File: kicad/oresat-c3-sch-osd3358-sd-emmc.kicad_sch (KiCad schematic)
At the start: 41 parts, among them J5 DM3BT-DSF-PEJS, U1 OSD3358-512M-BSM, U8 TCAN330, U9 EMMC+RESET+5.1-COMPATIBLE-BA

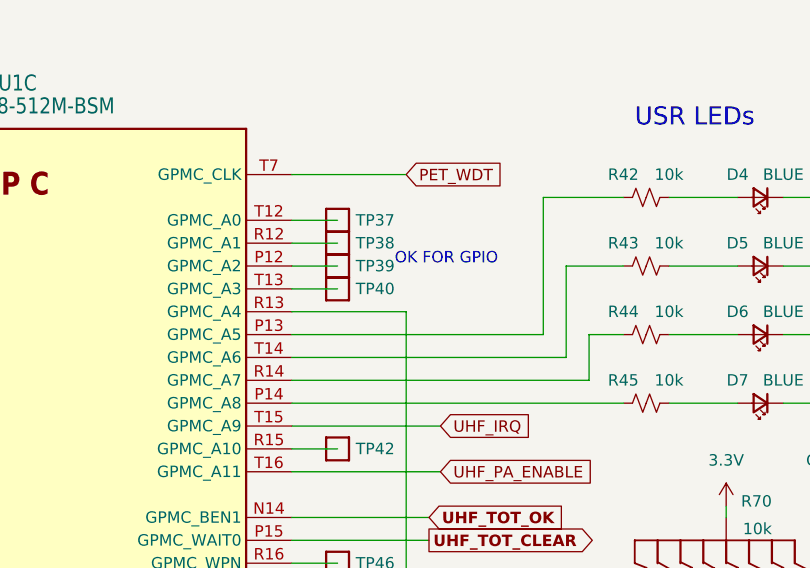
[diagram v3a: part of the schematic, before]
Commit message: routed everything but some minor lines and the radios. About to move the octavo and EVERYTHING else, wish me luck. Should give enough room for the radios!
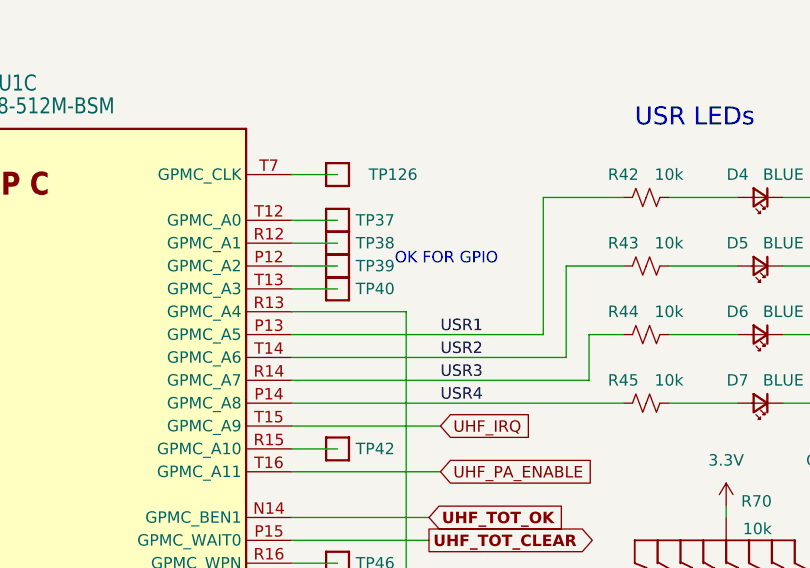
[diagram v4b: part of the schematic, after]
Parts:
- added TP126: Test-Point, oresat-misc:TestPoint_Pad_D1.0mm, symbol oresat-misc:Test-Point-1mm-round
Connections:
- net USR3: now reaches R44.1, U1.R14 (GPMC_A7)
- net USR1: now reaches R42.1, U1.P13 (GPMC_A5)
- net USR4: now reaches R45.1, U1.P14 (GPMC_A8)
- net USR2: now reaches R43.1, U1.T14 (GPMC_A6)
- net PET_WDT: no longer names the net of U1.T7 (GPMC_CLK)
- net PET_WDT: now also TP126.1
- new net: U9.A1 (NC), U9.A10 (NC), U9.A11 (NC), U9.A12 (NC), U9.A13 (NC), U9.A14 (NC), U9.A2 (NC), U9.A7 (NC), U9.A8 (NC), U9.A9 (NC)
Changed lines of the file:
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@@
+    (stroke (width 0) (type default))
+  )
+  (wire (pts (xy 223.52 101.6) (xy 228.6 101.6))
     (stroke (width 0) (type default))
   )
@@
   )
   (wire (pts (xy 101.6 129.54) (xy 83.82 129.54))
-    (stroke (width 0) (type default))
-  )
-  (wire (pts (xy 223.52 101.6) (xy 236.22 101.6))
     (stroke (width 0) (type default))
   )
@@
     (effects (font (size 1.27 1.27)) (justify left bottom))
   )
+  (label "USR3" (at 240.03 124.46 0) (fields_autoplaced)
+    (effects (font (size 1.27 1.27)) (justify left bottom))
+  )
+  (label "USR4" (at 240.03 127 0) (fields_autoplaced)
+    (effects (font (size 1.27 1.27)) (justify left bottom))
+  )
+  (label "USR2" (at 240.03 121.92 0) (fields_autoplaced)
+    (effects (font (size 1.27 1.27)) (justify left bottom))
+  )
+  (label "USR1" (at 240.03 119.38 0) (fields_autoplaced)
+    (effects (font (size 1.27 1.27)) (justify left bottom))
+  )
   (global_label "SPI1_CS" (shape input) (at 132.08 195.58 180) (fields_autoplaced)
     (effects (font (size 1.27 1.27)) (justify right))
@@
     (property "Intersheetrefs" "${INTERSHEET_REFS}" (at 138.3666 106.68 0)
       (effects (font (size 1.27 1.27)) (justify right))
-    )
-  )
-  (global_label "PET_WDT" (shape input) (at 236.22 101.6 0) (fields_autoplaced)
-    (effects (font (size 1.27 1.27)) (justify left))
-    (property "Intersheetrefs" "${INTERSHEET_REFS}" (at 247.169 101.6 0)
-      (effects (font (size 1.27 1.27)) (justify left))
     )
   )
@@
     )
   )
+  (symbol (lib_id "oresat-misc:Test-Point-1mm-round") (at 228.6 101.6 90) (unit 1)
+    (in_bom yes) (on_board yes) (dnp no)
+    (property "Reference" "TP126" (at 237.49 101.6 90)
+      (effects (font (size 1.27 1.27)) (justify left))
+    )
+    (property "Value" "Test-Point" (at 226.06 101.6 0)
+      (effects (font (size 1.27 1.27)) hide)
+    )
+    (property "Footprint" "oresat-misc:TestPoint_Pad_D1.0mm" (at 218.44 101.6 0)
+      (effects (font (size 1.27 1.27)) hide)
+    )
+    (property "Datasheet" "" (at 228.6 101.6 0)
+      (effects (font (size 1.27 1.27)) hide)
+    )
+    (pin "1")
+    (instances
+      (project "oresat-c3"
+        (path "/65d12cdd-c326-4033-9053-c59fa4e0b25e/0c732c1e-ab0d-41ac-9d77-9d7763333b6f"
+          (reference "TP126") (unit 1)
+        )
+        (path "/65d12cdd-c326-4033-9053-c59fa4e0b25e/f3d147ad-4cea-4d77-ae60-95882b03454e"
+          (reference "TP68") (unit 1)
+        )
+      )
+    )
+  )
   (symbol (lib_id "power:GND1") (at 55.88 153.67 0) (unit 1)
     (in_bom yes) (on_board yes) (dnp no)
@@
       (effects (font (size 1.27 1.27)) hide)
     )
+    (pin "A1")
+    (pin "A10")
+    (pin "A11")
+    (pin "A12")
+    (pin "A13")
+    (pin "A14")
+    (pin "A2")
     (pin "A3")
     (pin "A4")
     (pin "A5")
     (pin "A6")
+    (pin "A7")
+    (pin "A9")
     (pin "B2")
     (pin "B3")
@@
     (pin "P5")
     (pin "P6")
-    (instances
-      (project "oresat-c3"
+    (pin "A8")
+    (instances
+      (project "oresat-c3"

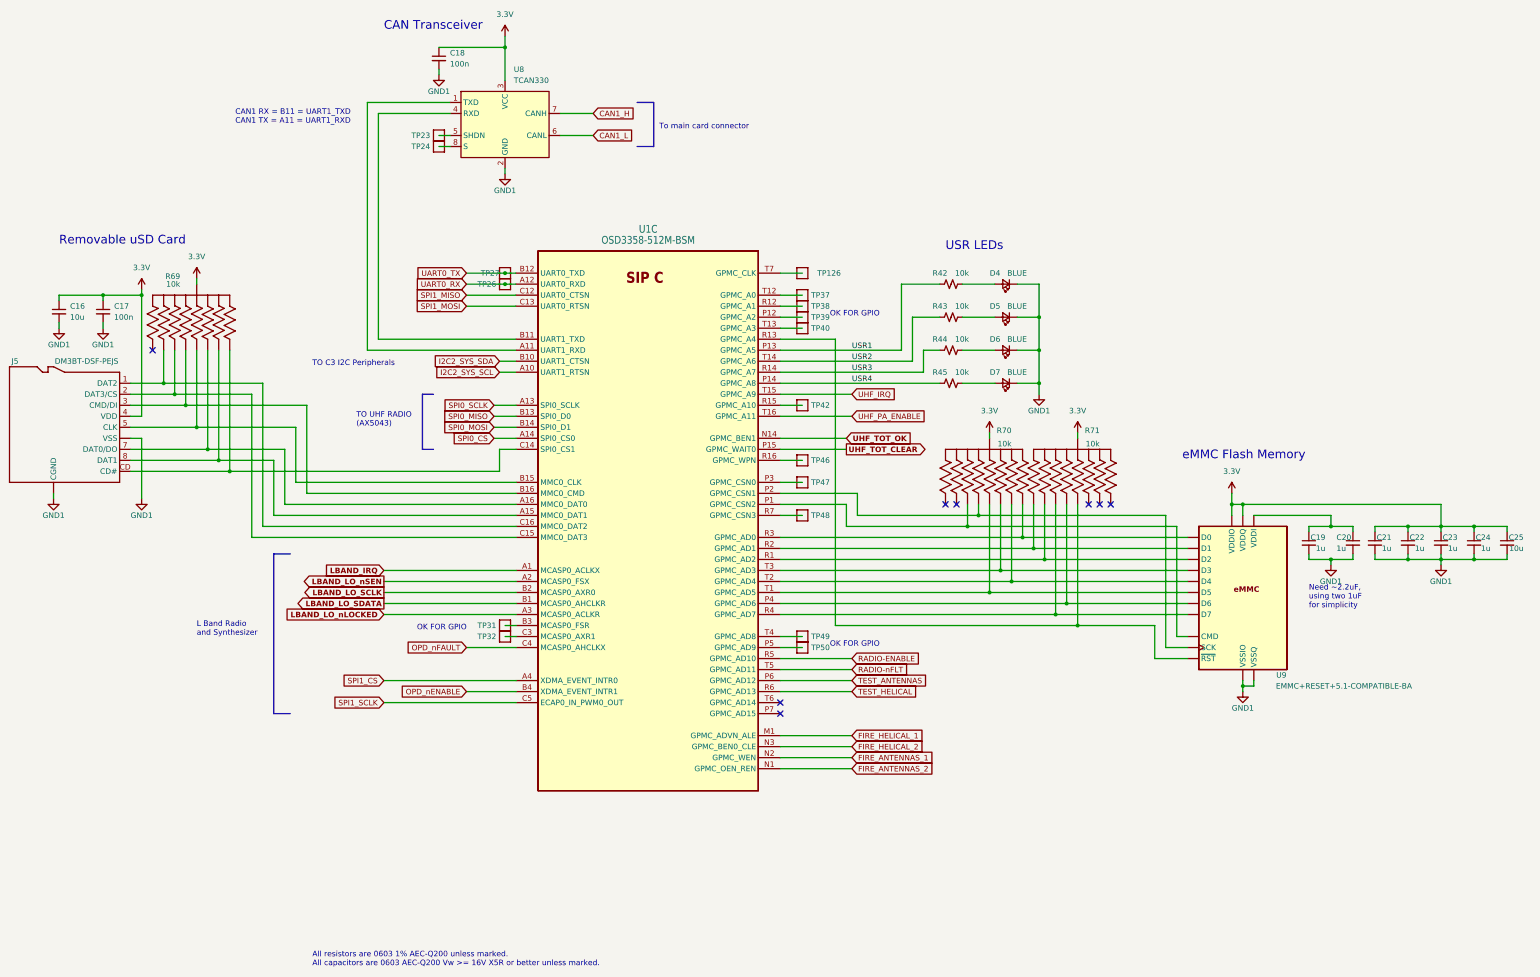
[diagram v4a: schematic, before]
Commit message: Switched all grounds to a single ground, because I can't find a way to overlap ground planes in KiCAD. That's actually not terrible, however, because KiCAD has an anti-plane feature which I used to cut the ground plane between UHF and L radios and L radio and Octavo. So actually I think it came out better than having separate ground planes. Only thing left now are the ~ 40 connections to the Octavo.
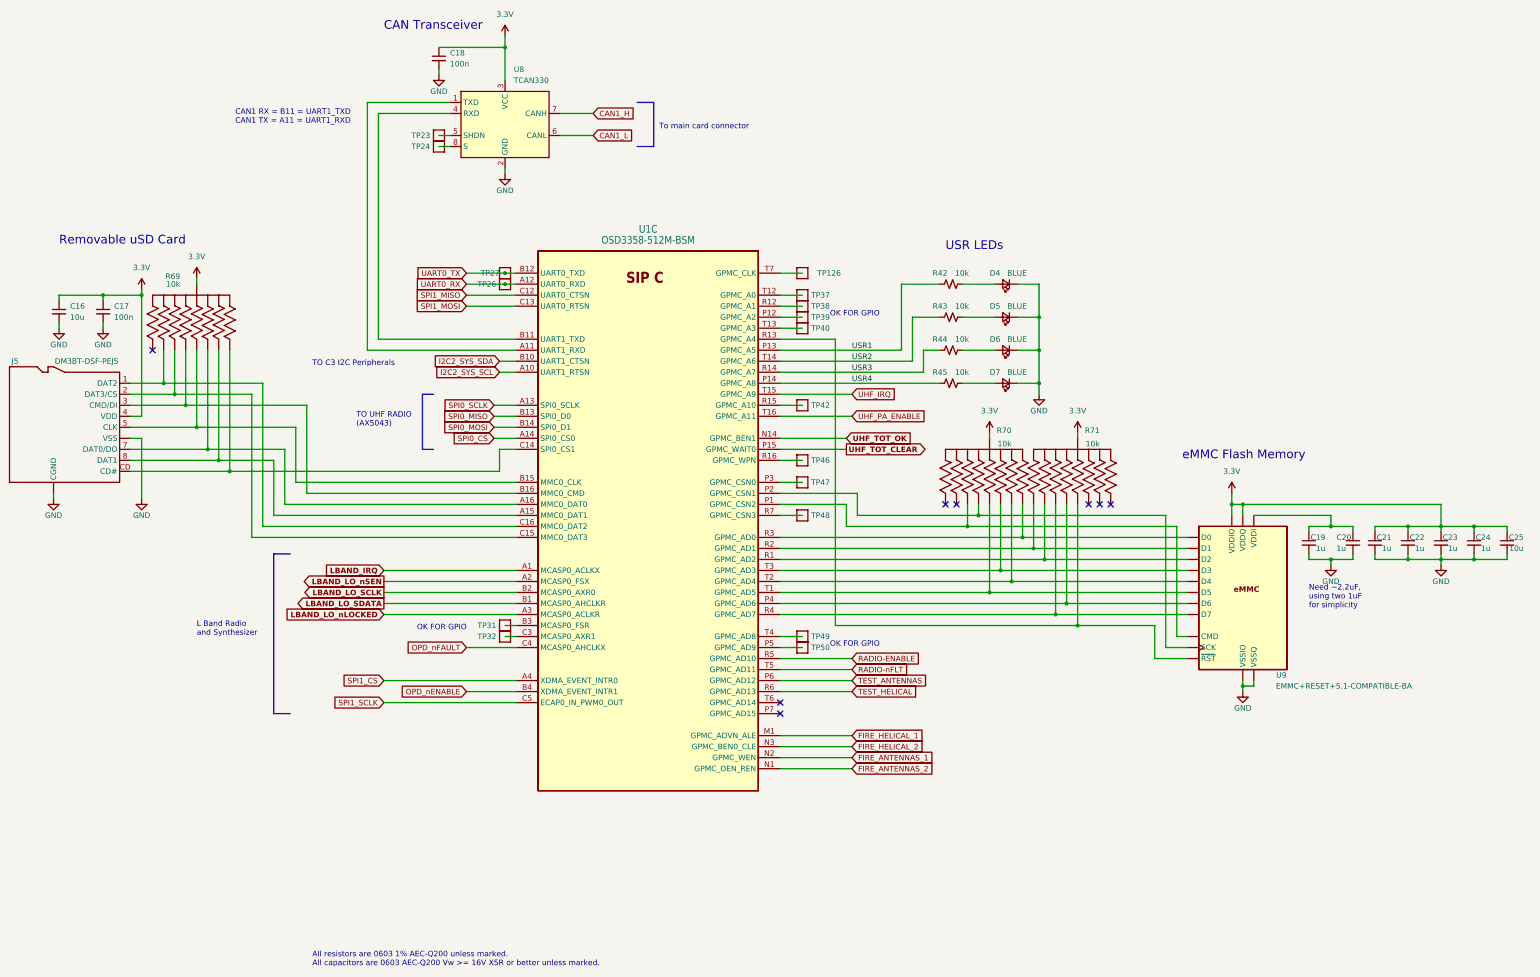
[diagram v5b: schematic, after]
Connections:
- net GND1 renamed GND
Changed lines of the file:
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@@
     )
   )
-  (symbol (lib_id "power:GND1") (at 375.92 168.91 0) (unit 1)
-    (in_bom yes) (on_board yes) (dnp no)
-    (property "Reference" "#PWR0149" (at 375.92 175.26 0)
-      (effects (font (size 1.27 1.27)) hide)
-    )
-    (property "Value" "GND1" (at 375.92 172.72 0)
+  (symbol (lib_id "power:GND") (at 375.92 168.91 0) (unit 1)
+    (in_bom yes) (on_board yes) (dnp no)
+    (property "Reference" "#PWR?" (at 375.92 175.26 0)
+      (effects (font (size 1.27 1.27)) hide)
+    )
+    (property "Value" "GND" (at 375.92 172.72 0)
       (effects (font (size 1.27 1.27)))
     )
@@
       (project "oresat-c3"
         (path "/65d12cdd-c326-4033-9053-c59fa4e0b25e/f3d147ad-4cea-4d77-ae60-95882b03454e"
-          (reference "#PWR0149") (unit 1)
+          (reference "#PWR?") (unit 1)
         )
       )
@@
     )
   )
-  (symbol (lib_id "power:GND1") (at 55.88 153.67 0) (unit 1)
-    (in_bom yes) (on_board yes) (dnp no)
-    (property "Reference" "#PWR0155" (at 55.88 160.02 0)
-      (effects (font (size 1.27 1.27)) hide)
-    )
-    (property "Value" "GND1" (at 55.88 157.48 0)
+  (symbol (lib_id "power:GND") (at 55.88 153.67 0) (unit 1)
+    (in_bom yes) (on_board yes) (dnp no)
+    (property "Reference" "#PWR?" (at 55.88 160.02 0)
+      (effects (font (size 1.27 1.27)) hide)
+    )
+    (property "Value" "GND" (at 55.88 157.48 0)
       (effects (font (size 1.27 1.27)))
     )
@@
       (project "oresat-c3"
         (path "/65d12cdd-c326-4033-9053-c59fa4e0b25e/f3d147ad-4cea-4d77-ae60-95882b03454e"
-          (reference "#PWR0155") (unit 1)
+          (reference "#PWR?") (unit 1)
         )
       )
@@
     )
   )
-  (symbol (lib_id "power:GND1") (at 283.21 129.54 0) (unit 1)
+  (symbol (lib_id "power:GND") (at 283.21 129.54 0) (unit 1)
     (in_bom yes) (on_board yes) (dnp no) (fields_autoplaced)
-    (property "Reference" "#PWR0148" (at 283.21 135.89 0)
-      (effects (font (size 1.27 1.27)) hide)
-    )
-    (property "Value" "GND1" (at 283.21 133.35 0)
+    (property "Reference" "#PWR?" (at 283.21 135.89 0)
+      (effects (font (size 1.27 1.27)) hide)
+    )
+    (property "Value" "GND" (at 283.21 133.35 0)
       (effects (font (size 1.27 1.27)))
     )
@@
       (project "oresat-c3"
         (path "/65d12cdd-c326-4033-9053-c59fa4e0b25e/f3d147ad-4cea-4d77-ae60-95882b03454e"
-          (reference "#PWR0148") (unit 1)
-        )
-      )
-    )
-  )
-  (symbol (lib_id "power:GND1") (at 76.2 153.67 0) (unit 1)
-    (in_bom yes) (on_board yes) (dnp no)
-    (property "Reference" "#PWR0156" (at 76.2 160.02 0)
-      (effects (font (size 1.27 1.27)) hide)
-    )
-    (property "Value" "GND1" (at 76.2 157.48 0)
+          (reference "#PWR?") (unit 1)
+        )
+      )
+    )
+  )
+  (symbol (lib_id "power:GND") (at 76.2 153.67 0) (unit 1)
+    (in_bom yes) (on_board yes) (dnp no)
+    (property "Reference" "#PWR?" (at 76.2 160.02 0)
+      (effects (font (size 1.27 1.27)) hide)
+    )
+    (property "Value" "GND" (at 76.2 157.48 0)
       (effects (font (size 1.27 1.27)))
     )
@@
       (project "oresat-c3"
         (path "/65d12cdd-c326-4033-9053-c59fa4e0b25e/f3d147ad-4cea-4d77-ae60-95882b03454e"
-          (reference "#PWR0156") (unit 1)
+          (reference "#PWR?") (unit 1)
         )
       )
@@
     )
   )
-  (symbol (lib_id "power:GND1") (at 350.52 168.91 0) (unit 1)
-    (in_bom yes) (on_board yes) (dnp no)
-    (property "Reference" "#PWR0151" (at 350.52 175.26 0)
-      (effects (font (size 1.27 1.27)) hide)
-    )
-    (property "Value" "GND1" (at 350.52 172.72 0)
+  (symbol (lib_id "power:GND") (at 350.52 168.91 0) (unit 1)
+    (in_bom yes) (on_board yes) (dnp no)
+    (property "Reference" "#PWR?" (at 350.52 175.26 0)
+      (effects (font (size 1.27 1.27)) hide)
+    )
+    (property "Value" "GND" (at 350.52 172.72 0)
       (effects (font (size 1.27 1.27)))
     )
@@
       (project "oresat-c3"
         (path "/65d12cdd-c326-4033-9053-c59fa4e0b25e/f3d147ad-4cea-4d77-ae60-95882b03454e"
-          (reference "#PWR0151") (unit 1)
-        )
-      )
-    )
-  )
-  (symbol (lib_id "power:GND1") (at 57.15 114.3 0) (unit 1)
-    (in_bom yes) (on_board yes) (dnp no)
-    (property "Reference" "#PWR0152" (at 57.15 120.65 0)
-      (effects (font (size 1.27 1.27)) hide)
-    )
-    (property "Value" "GND1" (at 57.15 118.11 0)
+          (reference "#PWR?") (unit 1)
+        )
+      )
+    )
+  )
+  (symbol (lib_id "power:GND") (at 57.15 114.3 0) (unit 1)
+    (in_bom yes) (on_board yes) (dnp no)
+    (property "Reference" "#PWR?" (at 57.15 120.65 0)
+      (effects (font (size 1.27 1.27)) hide)
+    )
+    (property "Value" "GND" (at 57.15 118.11 0)
       (effects (font (size 1.27 1.27)))
     )
@@
       (project "oresat-c3"
         (path "/65d12cdd-c326-4033-9053-c59fa4e0b25e/f3d147ad-4cea-4d77-ae60-95882b03454e"
-          (reference "#PWR0152") (unit 1)
+          (reference "#PWR?") (unit 1)
         )
       )
@@
     )
   )
-  (symbol (lib_id "power:GND1") (at 67.31 114.3 0) (unit 1)
-    (in_bom yes) (on_board yes) (dnp no)
-    (property "Reference" "#PWR0153" (at 67.31 120.65 0)
-      (effects (font (size 1.27 1.27)) hide)
-    )
-    (property "Value" "GND1" (at 67.31 118.11 0)
+  (symbol (lib_id "power:GND") (at 67.31 114.3 0) (unit 1)
+    (in_bom yes) (on_board yes) (dnp no)
+    (property "Reference" "#PWR?" (at 67.31 120.65 0)
+      (effects (font (size 1.27 1.27)) hide)
+    )
+    (property "Value" "GND" (at 67.31 118.11 0)
       (effects (font (size 1.27 1.27)))
     )
@@
       (project "oresat-c3"
         (path "/65d12cdd-c326-4033-9053-c59fa4e0b25e/f3d147ad-4cea-4d77-ae60-95882b03454e"
-          (reference "#PWR0153") (unit 1)
+          (reference "#PWR?") (unit 1)
         )
       )
@@
     )
   )
-  (symbol (lib_id "power:GND1") (at 160.02 78.74 0) (unit 1)
-    (in_bom yes) (on_board yes) (dnp no)
-    (property "Reference" "#PWR0157" (at 160.02 85.09 0)
-      (effects (font (size 1.27 1.27)) hide)
-    )
-    (property "Value" "GND1" (at 160.02 82.55 0)
+  (symbol (lib_id "power:GND") (at 160.02 78.74 0) (unit 1)
+    (in_bom yes) (on_board yes) (dnp no)
+    (property "Reference" "#PWR?" (at 160.02 85.09 0)
+      (effects (font (size 1.27 1.27)) hide)
+    )
+    (property "Value" "GND" (at 160.02 82.55 0)
       (effects (font (size 1.27 1.27)))
     )
@@
       (project "oresat-c3"
         (path "/65d12cdd-c326-4033-9053-c59fa4e0b25e/f3d147ad-4cea-4d77-ae60-95882b03454e"
-          (reference "#PWR0157") (unit 1)
+          (reference "#PWR?") (unit 1)
         )
       )
@@
     )
   )
-  (symbol (lib_id "power:GND1") (at 330.2 198.12 0) (unit 1)
-    (in_bom yes) (on_board yes) (dnp no)
-    (property "Reference" "#PWR0150" (at 330.2 204.47 0)
-      (effects (font (size 1.27 1.27)) hide)
-    )
-    (property "Value" "GND1" (at 330.2 201.93 0)
+  (symbol (lib_id "power:GND") (at 330.2 198.12 0) (unit 1)
+    (in_bom yes) (on_board yes) (dnp no)
+    (property "Reference" "#PWR?" (at 330.2 204.47 0)
+      (effects (font (size 1.27 1.27)) hide)
+    )
+    (property "Value" "GND" (at 330.2 201.93 0)
       (effects (font (size 1.27 1.27)))
     )
@@
       (project "oresat-c3"
         (path "/65d12cdd-c326-4033-9053-c59fa4e0b25e/f3d147ad-4cea-4d77-ae60-95882b03454e"
-          (reference "#PWR0150") (unit 1)
-        )
-      )
-    )
-  )
-  (symbol (lib_id "power:GND1") (at 144.78 55.88 0) (unit 1)
-    (in_bom yes) (on_board yes) (dnp no)
-    (property "Reference" "#PWR0154" (at 144.78 62.23 0)
-      (effects (font (size 1.27 1.27)) hide)
-    )
-    (property "Value" "GND1" (at 144.78 59.69 0)
+          (reference "#PWR?") (unit 1)
+        )
+      )
+    )
+  )
+  (symbol (lib_id "power:GND") (at 144.78 55.88 0) (unit 1)
+    (in_bom yes) (on_board yes) (dnp no)
+    (property "Reference" "#PWR?" (at 144.78 62.23 0)
+      (effects (font (size 1.27 1.27)) hide)
+    )
+    (property "Value" "GND" (at 144.78 59.69 0)
       (effects (font (size 1.27 1.27)))
     )
@@
       (project "oresat-c3"
         (path "/65d12cdd-c326-4033-9053-c59fa4e0b25e/f3d147ad-4cea-4d77-ae60-95882b03454e"
-          (reference "#PWR0154") (unit 1)
-        )
-      )
+          (reference "#PWR?") (unit 1)
+        )
+      )
